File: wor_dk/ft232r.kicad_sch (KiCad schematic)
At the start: 16 parts, among them J501 USB_C_Receptacle_USB2.0_14P, U501 FT232RL

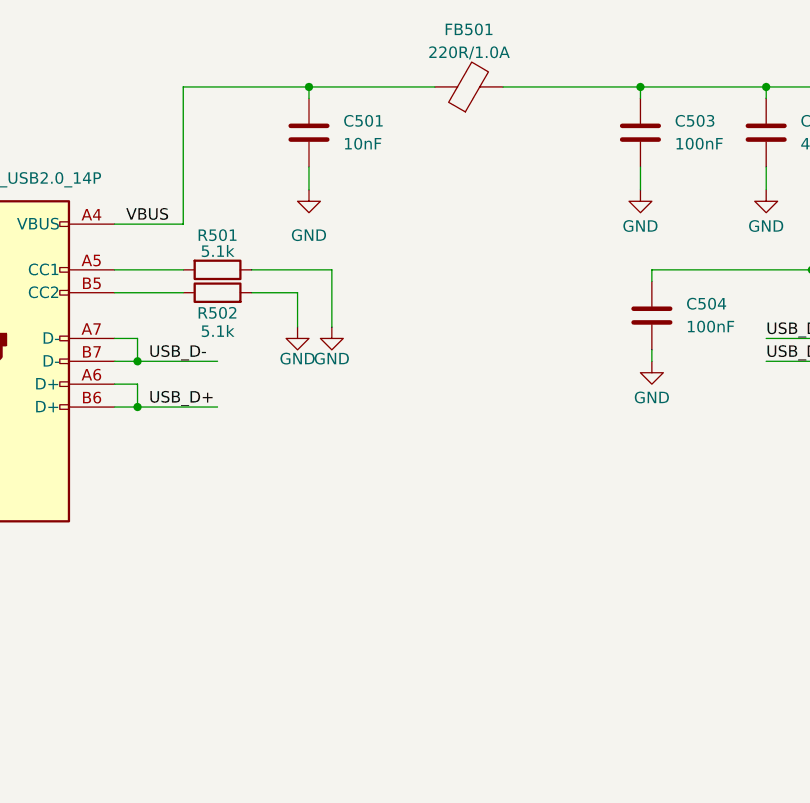
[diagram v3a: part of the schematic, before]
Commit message: wor_dk: FT232: add ESD protection for USB data lines
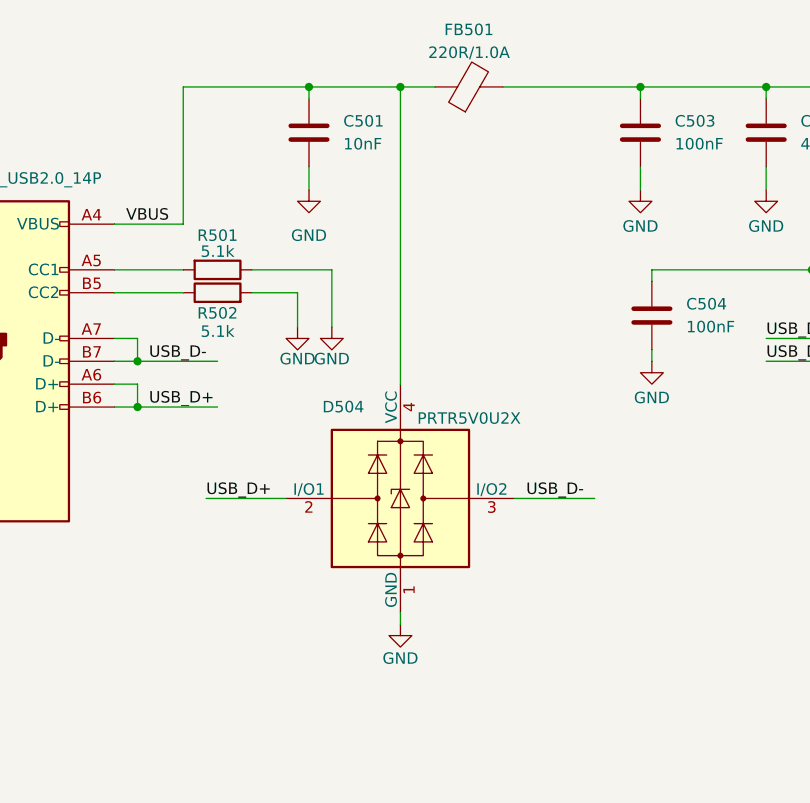
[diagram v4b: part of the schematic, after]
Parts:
- added D504: PRTR5V0U2X, Package_TO_SOT_SMD:SOT-143, symbol Power_Protection:PRTR5V0U2X
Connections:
- net GND: now also D504.1 (GND)
- net USB_D+: now also D504.2 (I/O1)
- net USB_D-: now also D504.3 (I/O2)
- net VBUS: now also D504.4 (VCC)
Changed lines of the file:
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@@
+		(color 0 0 0 0)
+	)
+	(junction
+		(at 127 60.96)
+		(diameter 0)
 		(color 0 0 0 0)
 	)
@@
 	(wire
 		(pts
+			(xy 105.41 106.68) (xy 114.3 106.68)
+		)
+		(stroke
+			(width 0)
+			(type default)
+		)
+	)
+	(wire
+		(pts
 			(xy 217.17 81.28) (xy 224.79 81.28)
 		)
@@
 	(wire
 		(pts
+			(xy 127 60.96) (xy 130.81 60.96)
+		)
+		(stroke
+			(width 0)
+			(type default)
+		)
+	)
+	(wire
+		(pts
 			(xy 172.72 72.39) (xy 172.72 81.28)
 		)
@@
 	(wire
 		(pts
+			(xy 127 60.96) (xy 127 93.98)
+		)
+		(stroke
+			(width 0)
+			(type default)
+		)
+	)
+	(wire
+		(pts
 			(xy 167.64 91.44) (xy 176.53 91.44)
 		)
@@
 	(wire
 		(pts
+			(xy 127 119.38) (xy 127 120.65)
+		)
+		(stroke
+			(width 0)
+			(type default)
+		)
+	)
+	(wire
+		(pts
 			(xy 80.01 114.3) (xy 80.01 128.27)
 		)
@@
 	(wire
 		(pts
-			(xy 116.84 60.96) (xy 130.81 60.96)
+			(xy 139.7 106.68) (xy 148.59 106.68)
+		)
+		(stroke
+			(width 0)
+			(type default)
+		)
+	)
+	(wire
+		(pts
+			(xy 116.84 60.96) (xy 127 60.96)
 		)
 		(stroke
@@
 	)
 	(label "USB_D-"
+		(at 140.97 106.68 0)
+		(fields_autoplaced yes)
+		(effects
+			(font
+				(size 1.27 1.27)
+			)
+			(justify left bottom)
+		)
+	)
+	(label "USB_D-"
 		(at 99.06 91.44 0)
+		(fields_autoplaced yes)
+		(effects
+			(font
+				(size 1.27 1.27)
+			)
+			(justify left bottom)
+		)
+	)
+	(label "USB_D+"
+		(at 105.41 106.68 0)
 		(fields_autoplaced yes)
 		(effects
@@
 	)
 	(symbol
+		(lib_id "Power_Protection:PRTR5V0U2X")
+		(at 127 106.68 0)
+		(unit 1)
+		(exclude_from_sim no)
+		(in_bom yes)
+		(on_board yes)
+		(dnp no)
+		(property "Reference" "D504"
+			(at 120.65 96.52 0)
+			(effects
+				(font
+					(size 1.27 1.27)
+				)
+			)
+		)
+		(property "Value" "PRTR5V0U2X"
+			(at 134.62 97.79 0)
+			(effects
+				(font
+					(size 1.27 1.27)
+				)
+			)
+		)
+		(property "Footprint" "Package_TO_SOT_SMD:SOT-143"
+			(at 128.524 106.68 0)
+			(effects
+				(font
+					(size 1.27 1.27)
+				)
+				(hide yes)
+			)
+		)
+		(property "Datasheet" "https://assets.nexperia.com/documents/data-sheet/PRTR5V0U2X.pdf"
+			(at 128.524 106.68 0)
+			(effects
+				(font
+					(size 1.27 1.27)
+				)
+				(hide yes)
+			)
+		)
+		(property "Description" ""
+			(at 127 106.68 0)
+			(effects
+				(font
+					(size 1.27 1.27)
+				)
+				(hide yes)
+			)
+		)
+		(property "LCSC" "C2827688"
+			(at 127 106.68 0)
+			(effects
+				(font
+					(size 1.27 1.27)
+				)
+				(hide yes)
+			)
+		)
+		(property "Manufacturer" "TECH PUBLIC"
+			(at 127 106.68 0)
+			(effects
+				(font
+					(size 1.27 1.27)
+				)
+				(hide yes)
+			)
+		)
+		(property "Part Number" "PRTR5V0U2X"
+			(at 127 106.68 0)
+			(effects
+				(font
+					(size 1.27 1.27)
+				)
+				(hide yes)
+			)
+		)
+		(pin "1"
+		)
+		(pin "2"
+		)
+		(pin "3"
+		)
+		(pin "4"
+		)
+		(instances
+			(project "wor_dk"
+				(path "/8d3147eb-060b-4f65-bf42-ed06a58b21ba/711499aa-b4ff-4669-a7c0-a5db1aab8120"
+					(reference "D504")
+					(unit 1)
+				)
+			)
+		)
+	)
+	(symbol
 		(lib_id "power:PWR_FLAG")
 		(at 196.85 60.96 0)
@@
 					(unit 1)
 				)
+			)
+		)
+	)
+	(symbol
+		(lib_id "power:GND")
+		(at 127 120.65 0)
+		(unit 1)
+		(exclude_from_sim no)
+		(in_bom yes)
+		(on_board yes)
+		(dnp no)
+		(property "Reference" "#PWR0511"
+			(at 127 127 0)
+			(effects
+				(font
+					(size 1.27 1.27)
+				)
+				(hide yes)
+			)
+		)
+		(property "Value" "GND"
+			(at 127 124.46 0)
+			(effects
+				(font
+					(size 1.27 1.27)
+				)
+			)
+		)
+		(property "Footprint" ""
+			(at 127 120.65 0)
+			(effects
+				(font
+					(size 1.27 1.27)
+				)
+				(hide yes)
+			)
+		)
+		(property "Datasheet" ""
+			(at 127 120.65 0)
+			(effects
+				(font
+					(size 1.27 1.27)
+				)
+				(hide yes)
+			)
+		)
+		(property "Description" "Power symbol creates a global label with name \"GND\" , ground"
+			(at 127 120.65 0)
+			(effects
+				(font
+					(size 1.27 1.27)
+				)
+				(hide yes)
+			)
+		)
+		(pin "1"
+		)
+		(instances
+			(project "wor_dk"
+				(path "/8d3147eb-060b-4f65-bf42-ed06a58b21ba/711499aa-b4ff-4669-a7c0-a5db1aab8120"
+					(reference "#PWR0511")
+					(unit 1)
+				)

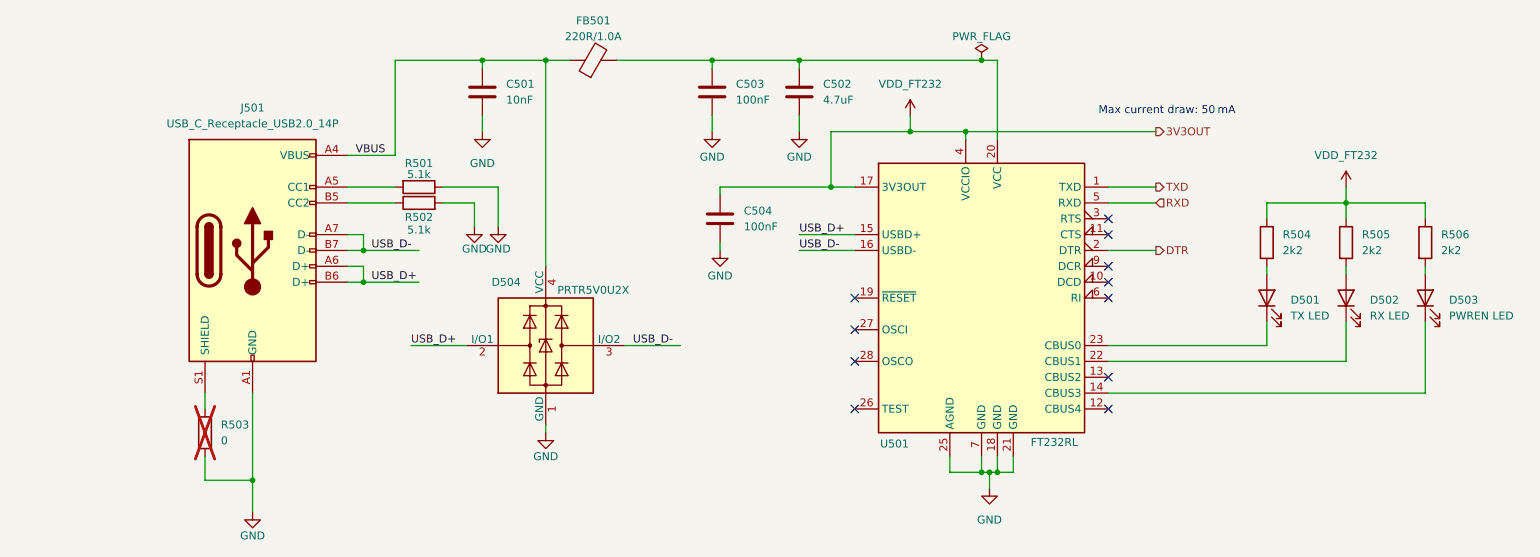
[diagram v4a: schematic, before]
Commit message: wor_dk: add 100 mA fuses for USB power
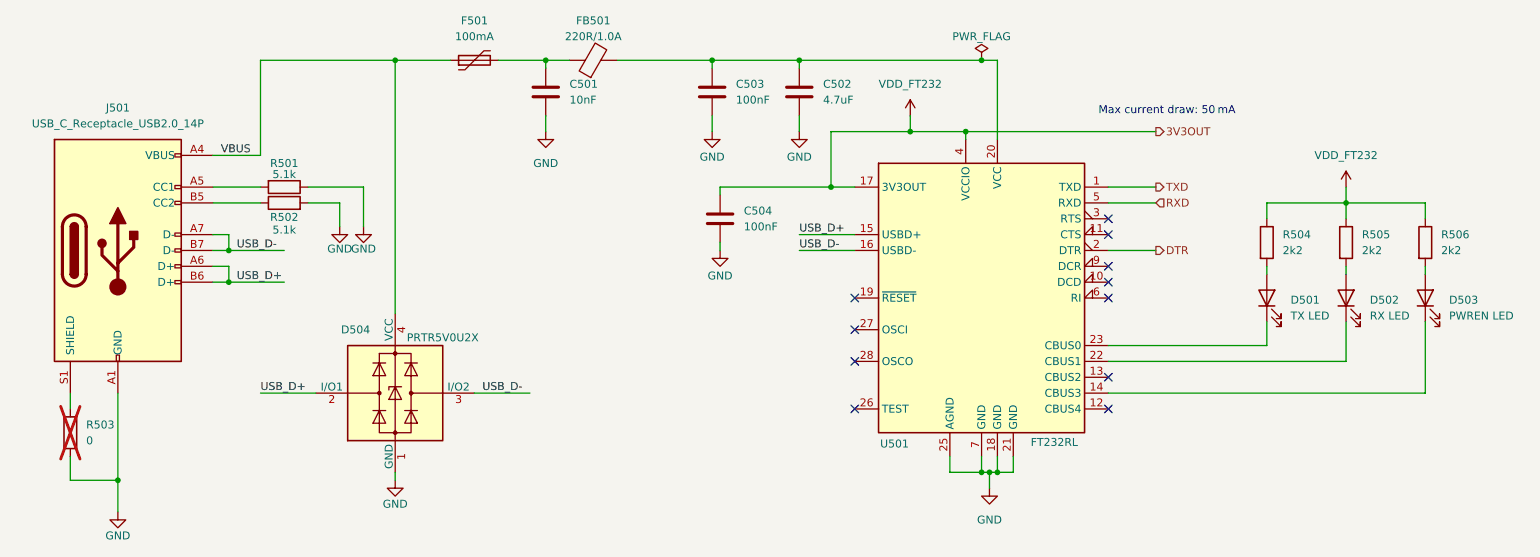
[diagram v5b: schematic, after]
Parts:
- added F501: 100mA, Fuse:Fuse_0603_1608Metric, symbol Device:Polyfuse
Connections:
- net VBUS: now also F501.1; no longer C501.1, FB501.1
- new net: C501.1, F501.2, FB501.1
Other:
- moved on the sheet: C501, D504, J501, R501, R502, R503

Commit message: wor_dk: remove controller & re-annotate schematics
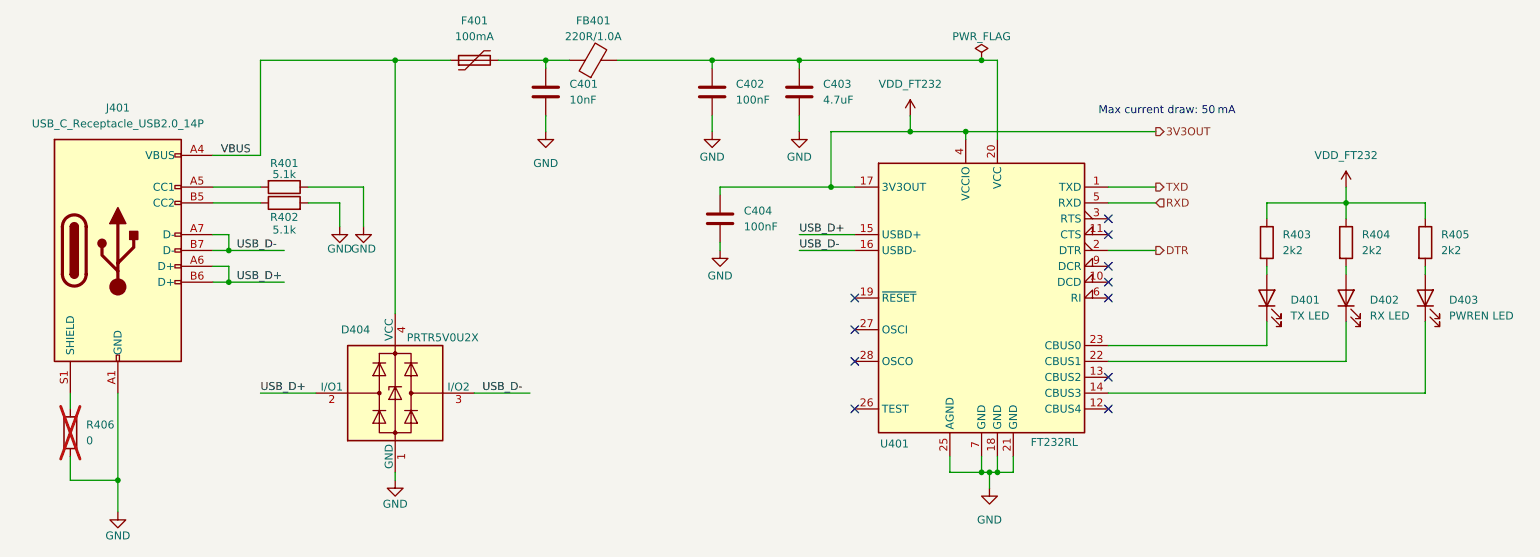
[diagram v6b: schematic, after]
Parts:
- renumbered C501 to C401, C503 to C402, C502 to C403, C504 to C404, D501 to D401, D502 to D402, D503 to D403, D504 to D404, F501 to F401, FB501 to FB401, J501 to J401, R501 to R401, R502 to R402, R504 to R403, R505 to R404, R506 to R405, R503 to R406, U501 to U401
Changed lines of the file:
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@@
 		(on_board yes)
 		(dnp no)
-		(property "Reference" "#PWR0501"
+		(property "Reference" "#PWR0407"
 			(at 97.79 93.98 0)
 			(effects
@@
 			(project ""
 				(path "/8d3147eb-060b-4f65-bf42-ed06a58b21ba/711499aa-b4ff-4669-a7c0-a5db1aab8120"
-					(reference "#PWR0501")
+					(reference "#PWR0407")
 					(unit 1)
 				)
@@
 		(dnp no)
 		(fields_autoplaced yes)
-		(property "Reference" "C501"
+		(property "Reference" "C401"
 			(at 130.81 64.7699 0)
 			(effects
@@
 			(project "wor_dk"
 				(path "/8d3147eb-060b-4f65-bf42-ed06a58b21ba/711499aa-b4ff-4669-a7c0-a5db1aab8120"
-					(reference "C501")
+					(reference "C401")
 					(unit 1)
 				)
@@
 		(dnp no)
 		(fields_autoplaced yes)
-		(property "Reference" "D501"
+		(property "Reference" "D401"
 			(at 246.38 99.3774 90)
 			(effects
@@
 			(project "wor_dk"
 				(path "/8d3147eb-060b-4f65-bf42-ed06a58b21ba/711499aa-b4ff-4669-a7c0-a5db1aab8120"
-					(reference "D501")
+					(reference "D401")
 					(unit 1)
 				)
@@
 		(on_board yes)
 		(dnp no)
-		(property "Reference" "U501"
+		(property "Reference" "U401"
 			(at 180.594 122.428 0)
 			(effects
@@
 			(project ""
 				(path "/8d3147eb-060b-4f65-bf42-ed06a58b21ba/711499aa-b4ff-4669-a7c0-a5db1aab8120"
-					(reference "U501")
+					(reference "U401")
 					(unit 1)
 				)
@@
 		(dnp no)
 		(fields_autoplaced yes)
-		(property "Reference" "D502"
+		(property "Reference" "D402"
 			(at 259.08 99.3774 90)
 			(effects
@@
 			(project "wor_dk"
 				(path "/8d3147eb-060b-4f65-bf42-ed06a58b21ba/711499aa-b4ff-4669-a7c0-a5db1aab8120"
-					(reference "D502")
+					(reference "D402")
 					(unit 1)
 				)
@@
 		(dnp no)
 		(fields_autoplaced yes)
-		(property "Reference" "#PWR0508"
+		(property "Reference" "#PWR0410"
 			(at 198.12 135.89 0)
 			(effects
@@
 			(project ""
 				(path "/8d3147eb-060b-4f65-bf42-ed06a58b21ba/711499aa-b4ff-4669-a7c0-a5db1aab8120"
-					(reference "#PWR0508")
+					(reference "#PWR0410")
 					(unit 1)
 				)
@@
 		(on_board yes)
 		(dnp no)
-		(property "Reference" "#PWR0506"
+		(property "Reference" "#PWR0404"
 			(at 167.64 78.74 0)
 			(effects
@@
 			(project "wor_dk"
 				(path "/8d3147eb-060b-4f65-bf42-ed06a58b21ba/711499aa-b4ff-4669-a7c0-a5db1aab8120"
-					(reference "#PWR0506")
+					(reference "#PWR0404")
 					(unit 1)
 				)
@@
 		(dnp no)
 		(fields_autoplaced yes)
-		(property "Reference" "C504"
+		(property "Reference" "C404"
 			(at 158.75 85.0899 0)
 			(effects
@@
 			(project "wor_dk"
 				(path "/8d3147eb-060b-4f65-bf42-ed06a58b21ba/711499aa-b4ff-4669-a7c0-a5db1aab8120"
-					(reference "C504")
+					(reference "C404")
 					(unit 1)
 				)
@@
 		(on_board yes)
 		(dnp no)
-		(property "Reference" "D504"
+		(property "Reference" "D404"
 			(at 96.52 104.14 0)
 			(effects
@@
 			(project "wor_dk"
 				(path "/8d3147eb-060b-4f65-bf42-ed06a58b21ba/711499aa-b4ff-4669-a7c0-a5db1aab8120"
-					(reference "D504")
+					(reference "D404")
 					(unit 1)
 				)
@@
 		(on_board yes)
 		(dnp no)
-		(property "Reference" "#FLG0501"
+		(property "Reference" "#FLG0401"
 			(at 196.85 59.055 0)
 			(effects
@@
 			(project "wor_dk"
 				(path "/8d3147eb-060b-4f65-bf42-ed06a58b21ba/711499aa-b4ff-4669-a7c0-a5db1aab8120"
-					(reference "#FLG0501")
+					(reference "#FLG0401")
 					(unit 1)
 				)
@@
 		(on_board yes)
 		(dnp no)
-		(property "Reference" "#PWR0503"
+		(property "Reference" "#PWR0411"
 			(at 58.42 139.7 0)
 			(effects
@@
 			(project ""
 				(path "/8d3147eb-060b-4f65-bf42-ed06a58b21ba/711499aa-b4ff-4669-a7c0-a5db1aab8120"
-					(reference "#PWR0503")
+					(reference "#PWR0411")
 					(unit 1)
 				)
@@
 		(dnp no)
 		(fields_autoplaced yes)
-		(property "Reference" "#PWR0504"
+		(property "Reference" "#PWR0402"
 			(at 127 78.74 0)
 			(effects
@@
 			(project ""
 				(path "/8d3147eb-060b-4f65-bf42-ed06a58b21ba/711499aa-b4ff-4669-a7c0-a5db1aab8120"
-					(reference "#PWR0504")
+					(reference "#PWR0402")
 					(unit 1)
 				)
@@
 		(dnp no)
 		(fields_autoplaced yes)
-		(property "Reference" "J501"
+		(property "Reference" "J401"
 			(at 58.42 68.58 0)
 			(effects
@@
 			(project ""
 				(path "/8d3147eb-060b-4f65-bf42-ed06a58b21ba/711499aa-b4ff-4669-a7c0-a5db1aab8120"
-					(reference "J501")
+					(reference "J401")
 					(unit 1)
 				)
@@
 		(dnp no)
 		(fields_autoplaced yes)
-		(property "Reference" "F501"
+		(property "Reference" "F401"
 			(at 115.57 54.61 90)
 			(effects
@@
 			(project "wor_dk"
 				(path "/8d3147eb-060b-4f65-bf42-ed06a58b21ba/711499aa-b4ff-4669-a7c0-a5db1aab8120"
-					(reference "F501")
+					(reference "F401")
 					(unit 1)
 				)
@@
 		(dnp yes)
 		(fields_autoplaced yes)
-		(property "Reference" "R503"
+		(property "Reference" "R406"
 			(at 53.34 119.3799 0)
 			(effects
@@
 			(project ""
 				(path "/8d3147eb-060b-4f65-bf42-ed06a58b21ba/711499aa-b4ff-4669-a7c0-a5db1aab8120"
-					(reference "R503")
+					(reference "R406")
 					(unit 1)
 				)
@@
 		(dnp no)
 		(fields_autoplaced yes)
-		(property "Reference" "C503"
+		(property "Reference" "C402"
 			(at 157.48 64.7699 0)
 			(effects
@@
 			(project "wor_dk"
 				(path "/8d3147eb-060b-4f65-bf42-ed06a58b21ba/711499aa-b4ff-4669-a7c0-a5db1aab8120"
-					(reference "C503")
+					(reference "C402")
 					(unit 1)
 				)
@@
 		(on_board yes)
 		(dnp no)
-		(property "Reference" "R502"
+		(property "Reference" "R402"
 			(at 85.09 86.106 90)
 			(effects
@@
 			(project ""
 				(path "/8d3147eb-060b-4f65-bf42-ed06a58b21ba/711499aa-b4ff-4669-a7c0-a5db1aab8120"
-					(reference "R502")
+					(reference "R402")
 					(unit 1)
 				)
@@
 		(on_board yes)
 		(dnp no)
-		(property "Reference" "R501"
+		(property "Reference" "R401"
 			(at 85.09 77.47 90)
 			(effects
@@
 			(project ""
 				(path "/8d3147eb-060b-4f65-bf42-ed06a58b21ba/711499aa-b4ff-4669-a7c0-a5db1aab8120"
-					(reference "R501")
+					(reference "R401")
 					(unit 1)
 				)
@@
 		(dnp no)
 		(fields_autoplaced yes)
-		(property "Reference" "D503"
+		(property "Reference" "D403"
 			(at 271.78 99.3774 90)
 			(effects
@@
 			(project "wor_dk"
 				(path "/8d3147eb-060b-4f65-bf42-ed06a58b21ba/711499aa-b4ff-4669-a7c0-a5db1aab8120"
-					(reference "D503")
+					(reference "D403")
 					(unit 1)
 				)
@@
 		(dnp no)
 		(fields_autoplaced yes)
-		(property "Reference" "#PWR0509"
+		(property "Reference" "#PWR0405"
 			(at 255.27 85.09 0)
 			(effects
@@
 			(project ""
 				(path "/8d3147eb-060b-4f65-bf42-ed06a58b21ba/711499aa-b4ff-4669-a7c0-a5db1aab8120"
-					(reference "#PWR0509")
+					(reference "#PWR0405")
 					(unit 1)
 				)
@@
 		(on_board yes)
 		(dnp no)
-		(property "Reference" "#PWR0507"
+		(property "Reference" "#PWR0408"
 			(at 154.94 97.79 0)
 			(effects
@@
 			(project "wor_dk"
 				(path "/8d3147eb-060b-4f65-bf42-ed06a58b21ba/711499aa-b4ff-4669-a7c0-a5db1aab8120"
-					(reference "#PWR0507")
+					(reference "#PWR0408")
 					(unit 1)
 				)
@@
 		(on_board yes)
 		(dnp no)
-		(property "Reference" "#PWR0502"
+		(property "Reference" "#PWR0406"
 			(at 93.98 93.98 0)
 			(effects
@@
 			(project ""
 				(path "/8d3147eb-060b-4f65-bf42-ed06a58b21ba/711499aa-b4ff-4669-a7c0-a5db1aab8120"
-					(reference "#PWR0502")
+					(reference "#PWR0406")
 					(unit 1)
 				)
@@
 		(dnp no)
 		(fields_autoplaced yes)
-		(property "Reference" "R506"
+		(property "Reference" "R405"
 			(at 270.51 88.8999 0)
 			(effects
@@
 			(project "wor_dk"
 				(path "/8d3147eb-060b-4f65-bf42-ed06a58b21ba/711499aa-b4ff-4669-a7c0-a5db1aab8120"
-					(reference "R506")
+					(reference "R405")
 					(unit 1)
 				)
@@
 		(dnp no)
 		(fields_autoplaced yes)
-		(property "Reference" "R504"
+		(property "Reference" "R403"
 			(at 245.11 88.8999 0)
 			(effects
@@
 			(project "wor_dk"
 				(path "/8d3147eb-060b-4f65-bf42-ed06a58b21ba/711499aa-b4ff-4669-a7c0-a5db1aab8120"
-					(reference "R504")
+					(reference "R403")
 					(unit 1)
 				)
@@
 		(dnp no)
 		(fields_autoplaced yes)
-		(property "Reference" "R505"
+		(property "Reference" "R404"
 			(at 257.81 88.8999 0)
 			(effects
@@
 			(project "wor_dk"
 				(path "/8d3147eb-060b-4f65-bf42-ed06a58b21ba/711499aa-b4ff-4669-a7c0-a5db1aab8120"
-					(reference "R505")
+					(reference "R404")
 					(unit 1)
 				)
@@
 		(on_board yes)
 		(dnp no)
-		(property "Reference" "#PWR0511"
+		(property "Reference" "#PWR0409"
 			(at 102.87 134.62 0)
 			(effects
@@
 			(project "wor_dk"
 				(path "/8d3147eb-060b-4f65-bf42-ed06a58b21ba/711499aa-b4ff-4669-a7c0-a5db1aab8120"
-					(reference "#PWR0511")
+					(reference "#PWR0409")
 					(unit 1)
 				)
@@
 		(on_board yes)
 		(dnp no)
-		(property "Reference" "#PWR0505"
+		(property "Reference" "#PWR0403"
 			(at 153.67 78.74 0)
 			(effects
@@
 			(project ""
 				(path "/8d3147eb-060b-4f65-bf42-ed06a58b21ba/711499aa-b4ff-4669-a7c0-a5db1aab8120"
-					(reference "#PWR0505")
+					(reference "#PWR0403")
 					(unit 1)
 				)
@@
 		(dnp no)
 		(fields_autoplaced yes)
-		(property "Reference" "#PWR0510"
+		(property "Reference" "#PWR0401"
 			(at 185.42 73.66 0)
 			(effects
@@
 			(project "wor_dk"
 				(path "/8d3147eb-060b-4f65-bf42-ed06a58b21ba/711499aa-b4ff-4669-a7c0-a5db1aab8120"
-					(reference "#PWR0510")
+					(reference "#PWR0401")
 					(unit 1)
 				)
@@
 		(dnp no)
 		(fields_autoplaced yes)
-		(property "Reference" "C502"
+		(property "Reference" "C403"
 			(at 171.45 64.7699 0)
 			(effects
@@
 			(project "wor_dk"
 				(path "/8d3147eb-060b-4f65-bf42-ed06a58b21ba/711499aa-b4ff-4669-a7c0-a5db1aab8120"
-					(reference "C502")
+					(reference "C403")
 					(unit 1)
 				)
@@
 		(on_board yes)
 		(dnp no)
-		(property "Reference" "FB501"
+		(property "Reference" "FB401"
 			(at 134.62 54.61 90)
 			(effects
@@
 			(project "wor_dk"
 				(path "/8d3147eb-060b-4f65-bf42-ed06a58b21ba/711499aa-b4ff-4669-a7c0-a5db1aab8120"
-					(reference "FB501")
-					(unit 1)
-				)
+					(reference "FB401")
+					(unit 1)
+				)
